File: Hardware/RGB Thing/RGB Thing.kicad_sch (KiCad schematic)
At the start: 9 parts, among them J1 JST_SH_BM048, J2 UPDI Connection, U1 ATtiny1617

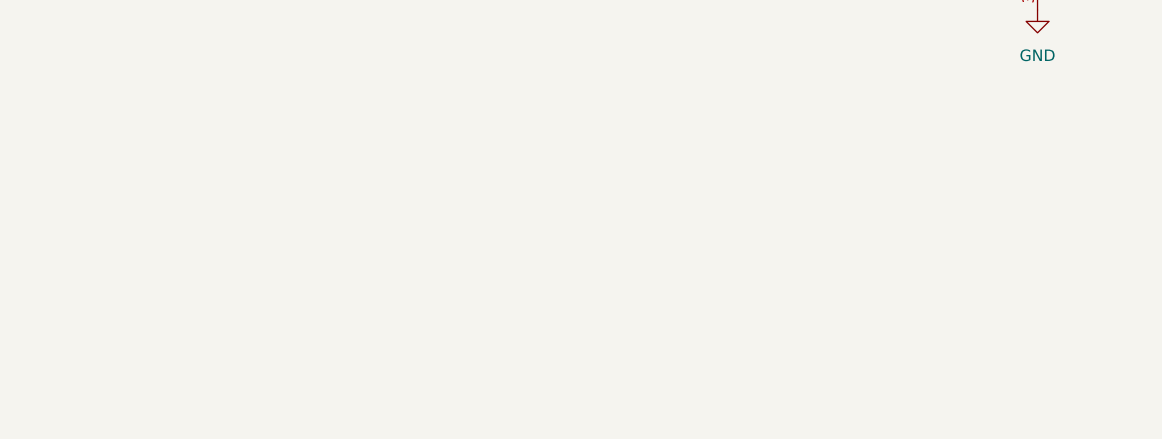
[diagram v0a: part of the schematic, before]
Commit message: Eliminated useless test points... and... NOW WITH RGB!!!
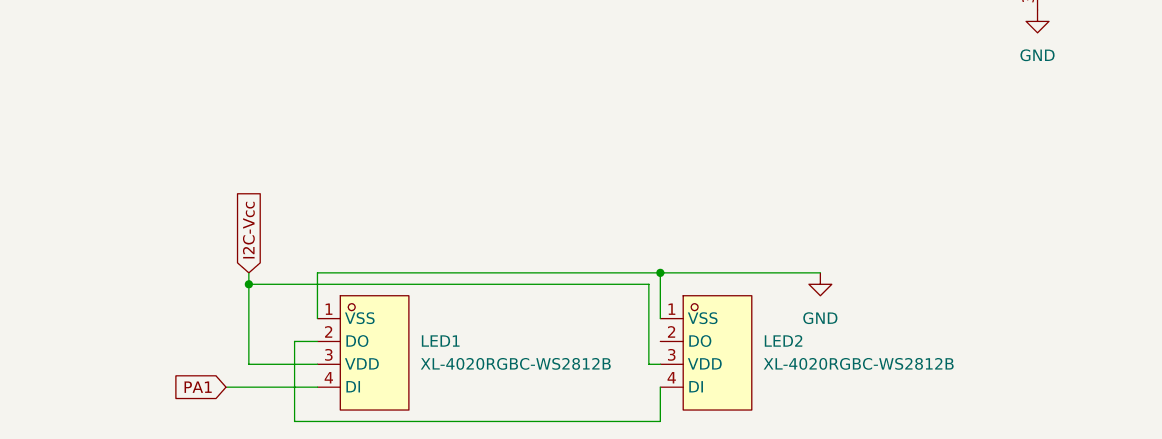
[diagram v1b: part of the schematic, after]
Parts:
- added LED1, LED2: XL-4020RGBC-WS2812B, tinker:LED-SMD_4P-L4.0-W1.7_XL-4020RGBC-WS2812B, symbol New_Library:XL-4020RGBC-WS2812B
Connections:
- net GND: now also LED1.1 (VSS), LED2.1 (VSS)
- net I2C-Vcc: now also LED1.3 (VDD), LED2.3 (VDD)
- net PA1: now also LED1.4 (DI)
- new net: LED1.2 (DO), LED2.4 (DI)
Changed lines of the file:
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@@
   (junction (at 184.15 80.01) (diameter 0) (color 0 0 0 0)
   )
+  (junction (at 62.23 135.89) (diameter 0) (color 0 0 0 0)
+  )
   (junction (at 171.45 57.15) (diameter 0) (color 0 0 0 0)
   )
   (junction (at 175.26 82.55) (diameter 0) (color 0 0 0 0)
   )
+  (junction (at 107.95 134.62) (diameter 0) (color 0 0 0 0)
+  )
   (junction (at 109.22 41.91) (diameter 0) (color 0 0 0 0)
   )
   (junction (at 149.86 41.91) (diameter 0) (color 0 0 0 0)
   )
+  (wire (pts (xy 62.23 144.78) (xy 62.23 135.89))
+    (stroke (width 0) (type default) (color 0 0 0 0))
+  )
   (wire (pts (xy 171.45 52.07) (xy 171.45 57.15))
     (stroke (width 0) (type default) (color 0 0 0 0))
   )
+  (wire (pts (xy 107.95 151.13) (xy 107.95 147.32))
+    (stroke (width 0) (type default) (color 0 0 0 0))
+  )
   (wire (pts (xy 186.69 57.15) (xy 189.23 57.15))
     (stroke (width 0) (type default) (color 0 0 0 0))
   )
+  (wire (pts (xy 69.85 134.62) (xy 69.85 139.7))
+    (stroke (width 0) (type default) (color 0 0 0 0))
+  )
   (wire (pts (xy 95.25 41.91) (xy 109.22 41.91))
     (stroke (width 0) (type default) (color 0 0 0 0))
@@
     (stroke (width 0) (type default) (color 0 0 0 0))
   )
+  (wire (pts (xy 107.95 139.7) (xy 107.95 134.62))
+    (stroke (width 0) (type default) (color 0 0 0 0))
+  )
   (wire (pts (xy 175.26 71.12) (xy 184.15 71.12))
     (stroke (width 0) (type default) (color 0 0 0 0))
   )
+  (wire (pts (xy 59.69 147.32) (xy 69.85 147.32))
+    (stroke (width 0) (type default) (color 0 0 0 0))
+  )
   (wire (pts (xy 175.26 78.74) (xy 175.26 82.55))
     (stroke (width 0) (type default) (color 0 0 0 0))
@@
     (stroke (width 0) (type default) (color 0 0 0 0))
   )
+  (wire (pts (xy 107.95 144.78) (xy 106.68 144.78))
+    (stroke (width 0) (type default) (color 0 0 0 0))
+  )
+  (wire (pts (xy 69.85 134.62) (xy 107.95 134.62))
+    (stroke (width 0) (type default) (color 0 0 0 0))
+  )
+  (wire (pts (xy 106.68 144.78) (xy 106.68 135.89))
+    (stroke (width 0) (type default) (color 0 0 0 0))
+  )
   (wire (pts (xy 184.15 78.74) (xy 184.15 80.01))
     (stroke (width 0) (type default) (color 0 0 0 0))
@@
     (stroke (width 0) (type default) (color 0 0 0 0))
   )
+  (wire (pts (xy 67.31 142.24) (xy 67.31 151.13))
+    (stroke (width 0) (type default) (color 0 0 0 0))
+  )
   (wire (pts (xy 184.15 80.01) (xy 165.1 80.01))
     (stroke (width 0) (type default) (color 0 0 0 0))
@@
     (stroke (width 0) (type default) (color 0 0 0 0))
   )
+  (wire (pts (xy 107.95 134.62) (xy 125.73 134.62))
+    (stroke (width 0) (type default) (color 0 0 0 0))
+  )
   (wire (pts (xy 165.1 57.15) (xy 171.45 57.15))
     (stroke (width 0) (type default) (color 0 0 0 0))
@@
     (stroke (width 0) (type default) (color 0 0 0 0))
   )
+  (wire (pts (xy 69.85 142.24) (xy 67.31 142.24))
+    (stroke (width 0) (type default) (color 0 0 0 0))
+  )
   (wire (pts (xy 175.26 82.55) (xy 165.1 82.55))
     (stroke (width 0) (type default) (color 0 0 0 0))
   )
+  (wire (pts (xy 62.23 135.89) (xy 106.68 135.89))
+    (stroke (width 0) (type default) (color 0 0 0 0))
+  )
   (wire (pts (xy 193.04 80.01) (xy 184.15 80.01))
     (stroke (width 0) (type default) (color 0 0 0 0))
   )
+  (wire (pts (xy 67.31 151.13) (xy 107.95 151.13))
+    (stroke (width 0) (type default) (color 0 0 0 0))
+  )
+  (wire (pts (xy 62.23 135.89) (xy 62.23 134.62))
+    (stroke (width 0) (type default) (color 0 0 0 0))
+  )
   (wire (pts (xy 165.1 85.09) (xy 182.88 85.09))
     (stroke (width 0) (type default) (color 0 0 0 0))
@@
   )
   (wire (pts (xy 27.94 45.72) (xy 27.94 33.02))
+    (stroke (width 0) (type default) (color 0 0 0 0))
+  )
+  (wire (pts (xy 69.85 144.78) (xy 62.23 144.78))
     (stroke (width 0) (type default) (color 0 0 0 0))
   )
@@
     )
   )
+  (global_label "PA1" (shape input) (at 59.69 147.32 180) (fields_autoplaced)
+    (effects (font (size 1.27 1.27)) (justify right))
+    (property "Intersheet References" "${INTERSHEET_REFS}" (id 0) (at 53.7977 147.3994 0)
+      (effects (font (size 1.27 1.27)) (justify right) hide)
+    )
+  )
   (global_label "PC5" (shape input) (at 134.62 92.71 180) (fields_autoplaced)
     (effects (font (size 1.27 1.27)) (justify right))
@@
     (property "Intersheet References" "${INTERSHEET_REFS}" (id 0) (at 33.4493 40.5606 0)
       (effects (font (size 1.27 1.27)) (justify right) hide)
+    )
+  )
+  (global_label "I2C-Vcc" (shape input) (at 62.23 134.62 90) (fields_autoplaced)
+    (effects (font (size 1.27 1.27)) (justify left))
+    (property "Intersheet References" "${INTERSHEET_REFS}" (id 0) (at -1.27 62.23 0)
+      (effects (font (size 1.27 1.27)) hide)
     )
   )
@@
     (pin "1")
     (pin "2")
+  )
+  (symbol (lib_id "New_Library:XL-4020RGBC-WS2812B") (at 76.2 143.51 0) (unit 1)
+    (in_bom yes) (on_board yes) (fields_autoplaced)
+    (property "Reference" "LED1" (id 0) (at 81.28 142.2399 0)
+      (effects (font (size 1.27 1.27)) (justify left))
+    )
+    (property "Value" "XL-4020RGBC-WS2812B" (id 1) (at 81.28 144.7799 0)
+      (effects (font (size 1.27 1.27)) (justify left))
+    )
+    (property "Footprint" "tinker:LED-SMD_4P-L4.0-W1.7_XL-4020RGBC-WS2812B" (id 2) (at 76.2 154.94 0)
+      (effects (font (size 1.27 1.27)) hide)
+    )
+    (property "Datasheet" "" (id 3) (at 76.2 143.51 0)
+      (effects (font (size 1.27 1.27)) hide)
+    )
+    (property "LCSC Part" "C3647024" (id 4) (at 76.2 157.48 0)
+      (effects (font (size 1.27 1.27)) hide)
+    )
+    (pin "1")
+    (pin "2")
+    (pin "3")
+    (pin "4")
   )
   (symbol (lib_id "MCU_Microchip_ATtiny:ATtiny817-M") (at 149.86 77.47 0) (unit 1)
@@
     (pin "9")
   )
+  (symbol (lib_id "New_Library:XL-4020RGBC-WS2812B") (at 114.3 143.51 0) (unit 1)
+    (in_bom yes) (on_board yes) (fields_autoplaced)
+    (property "Reference" "LED2" (id 0) (at 119.38 142.2399 0)
+      (effects (font (size 1.27 1.27)) (justify left))
+    )
+    (property "Value" "XL-4020RGBC-WS2812B" (id 1) (at 119.38 144.7799 0)
+      (effects (font (size 1.27 1.27)) (justify left))
+    )
+    (property "Footprint" "tinker:LED-SMD_4P-L4.0-W1.7_XL-4020RGBC-WS2812B" (id 2) (at 114.3 154.94 0)
+      (effects (font (size 1.27 1.27)) hide)
+    )
+    (property "Datasheet" "" (id 3) (at 114.3 143.51 0)
+      (effects (font (size 1.27 1.27)) hide)
+    )
+    (property "LCSC Part" "C3647024" (id 4) (at 114.3 157.48 0)
+      (effects (font (size 1.27 1.27)) hide)
+    )
+    (pin "1")
+    (pin "2")
+    (pin "3")
+    (pin "4")
+  )
   (symbol (lib_id "Device:R") (at 171.45 48.26 0) (unit 1)
     (in_bom yes) (on_board yes) (fields_autoplaced)
@@
     (pin "4")
     (pin "MP")
+  )
+  (symbol (lib_id "power:GND") (at 125.73 134.62 0) (unit 1)
+    (in_bom yes) (on_board yes) (fields_autoplaced)
+    (property "Reference" "#PWR0108" (id 0) (at 125.73 140.97 0)
+      (effects (font (size 1.27 1.27)) hide)
+    )
+    (property "Value" "GND" (id 1) (at 125.73 139.7 0))
+    (property "Footprint" "" (id 2) (at 125.73 134.62 0)
+      (effects (font (size 1.27 1.27)) hide)
+    )
+    (property "Datasheet" "" (id 3) (at 125.73 134.62 0)
+      (effects (font (size 1.27 1.27)) hide)
+    )
+    (pin "1")
   )
   (symbol (lib_id "Device:R") (at 182.88 57.15 90) (unit 1)
@@
       (reference "#PWR0106") (unit 1) (value "GND") (footprint "")
     )
+    (path "/bf3fd3b8-97f3-4ce0-a707-c2e87c85c69b"
+      (reference "#PWR0108") (unit 1) (value "GND") (footprint "")
+    )
     (path "/2486cc8e-3858-4480-8d7b-db0765931253"
       (reference "C1") (unit 1) (value "4.7uF") (footprint "Capacitor_SMD:C_0805_2012Metric")
@@
       (reference "J2") (unit 1) (value "UPDI Connection") (footprint "tinker:UPDI_connection")
     )
+    (path "/30ffb716-a88a-4539-a923-d855fc714029"
+      (reference "LED1") (unit 1) (value "XL-4020RGBC-WS2812B") (footprint "tinker:LED-SMD_4P-L4.0-W1.7_XL-4020RGBC-WS2812B")
+    )
+    (path "/39ce6e22-aa3a-4357-90c2-2275387430a5"
+      (reference "LED2") (unit 1) (value "XL-4020RGBC-WS2812B") (footprint "tinker:LED-SMD_4P-L4.0-W1.7_XL-4020RGBC-WS2812B")
+    )
     (path "/3eca1525-da26-4e2e-8484-417dd0ab3968"
